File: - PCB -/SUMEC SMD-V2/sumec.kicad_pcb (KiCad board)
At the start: 2 copper layers, 48 parts, among them J1 Conn_01x04_Pin, J2 Conn_01x01_Pin, J3 Conn_01x03_Pin, J6 Conn_01x06_Pin, J7 Conn_01x06_Pin, J8 TSOP382xx, J9 Conn_01x06_Pin, SW1 SW_Push, SW2 SW_Push, SW3 SW_Push, SW4 SW_DPDT_x2, U1 TB6612FNG, U3 USBLC6-2SC6, U7 LM1084IS-5.0/NOPB, U8 LM1084IS-3.3/NOPB

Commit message: sumec SMD V2 schematic update
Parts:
- removed D2: 1N5819, Diode_SMD:D_1206_3216Metric
- removed J1: Conn_01x04_Pin, Connector_PinHeader_2.54mm:PinHeader_1x04_P2.54mm_Vertical
- removed J6, J7, J9: Conn_01x06_Pin, Connector_JST:JST_SH_BM06B-SRSS-TB_1x06-1MP_P1.00mm_Vertical
- removed J8: TSOP382xx, Connector_PinSocket_2.54mm:PinSocket_1x03_P2.54mm_Vertical
- removed JP1: SolderJumper_3_Open, Jumper:SolderJumper-3_P2.0mm_Open_TrianglePad1.0x1.5mm
- removed R10, R11, R12, R13, R4, R8, R9: 0R, Resistor_SMD:R_1206_3216Metric
- removed R14, R16, R18: 100, Resistor_SMD:R_1206_3216Metric
- removed R15, R17, R19: 10k, Resistor_SMD:R_1206_3216Metric
- removed R3: 220, Resistor_SMD:R_1206_3216Metric_Pad1.30x1.75mm_HandSolder
- removed R5, R6: 15R, Resistor_SMD:R_1206_3216Metric
- removed R7: 10k.mcu, Resistor_SMD:R_1206_3216Metric
- added C10: 10uF.stabl, Capacitor_SMD:CP_Elec_4x5.8, F.Cu at (127.2, 26.8)
- added C11: 10uF.stabl, Capacitor_SMD:CP_Elec_4x5.8, F.Cu at (127.2, 32.6)
- added C12: 10uF.stabl, Capacitor_SMD:CP_Elec_4x5.8, F.Cu at (127.2, 38.5)
- added C13: 10uF.stabl, Capacitor_SMD:CP_Elec_4x5.8, F.Cu at (127.2, 44.4)
- added IC1: XT30U-F, sumec-smdV2_library:XT30U-M_1x02_P5.0mm_Vertical, F.Cu at (127.0, 50.9)
- added J10: Conn_01x03_Pin, Connector_PinHeader_2.54mm:PinHeader_1x03_P2.54mm_Vertical, F.Cu at (126.2, 72.8)
- added J11: Conn_01x03_Pin, Connector_PinHeader_2.54mm:PinHeader_1x03_P2.54mm_Vertical, F.Cu at (130.8, 72.8)
- added J4: Conn_01x04_Pin, Connector_Molex:Molex_PicoBlade_53398-0471_1x04-1MP_P1.25mm_Vertical, F.Cu at (130.4, 66.4)
- added U4: MPU-9250, Sensor_Motion:InvenSense_QFN-24_3x3mm_P0.4mm, F.Cu at (135.8, 73.0)
- added U5: TSOP382xx, Connector_PinSocket_2.54mm:PinSocket_1x03_P2.54mm_Vertical, F.Cu at (139.2, 58.9)
- H1, H2, H3, H4: value MountingHole M3 -> MountingHole_Pad; footprint MountingHole:MountingHole_3.2mm_M3_ISO7380_Pad -> MountingHole:MountingHole_3.2mm_M3_Pad
- J3: value Conn_01x03_Pin -> Conn_01x04_Pin; footprint Connector_PinSocket_2.54mm:PinSocket_1x03_P2.54mm_Vertical -> Connector_Molex:Molex_PicoBlade_53398-0471_1x04-1MP_P1.25mm_Vertical
- moved SW4 92.3 mm to (100.2, 26.2)
- moved SW1 78.5 mm to (100.8, 35.8)
- moved J2 75.5 mm to (99.7, 39.8)
- moved H1 72.2 mm to (93.8, 27.9)
- moved H2 71.9 mm to (93.8, 35.8)
- moved H3 71.6 mm to (93.8, 43.8)
- moved U7 71.3 mm to (116.4, 30.1)
- moved U8 71.3 mm to (116.4, 42.4)
- moved H4 71.3 mm to (93.8, 51.7)
- moved J3 51.2 mm to (130.4, 59.5)
- moved U3 35.6 mm to (114.8, 77.5)
- moved SW2 35.6 mm to (114.2, 68.8)
- moved SW3 35.6 mm to (114.2, 73.1)
- moved U1 31.8 mm to (116.6, 61.5)
- moved D1 28.7 mm to (114.3, 81.4)
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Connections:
- H1 pad 1: (no net) -> GND
- H2 pad 1: (no net) -> GND
- H3 pad 1: (no net) -> GND
- H4 pad 1: (no net) -> GND
- J3 pad 2: GND -> +3V3
- J3 pad 3: +3V3 -> GND

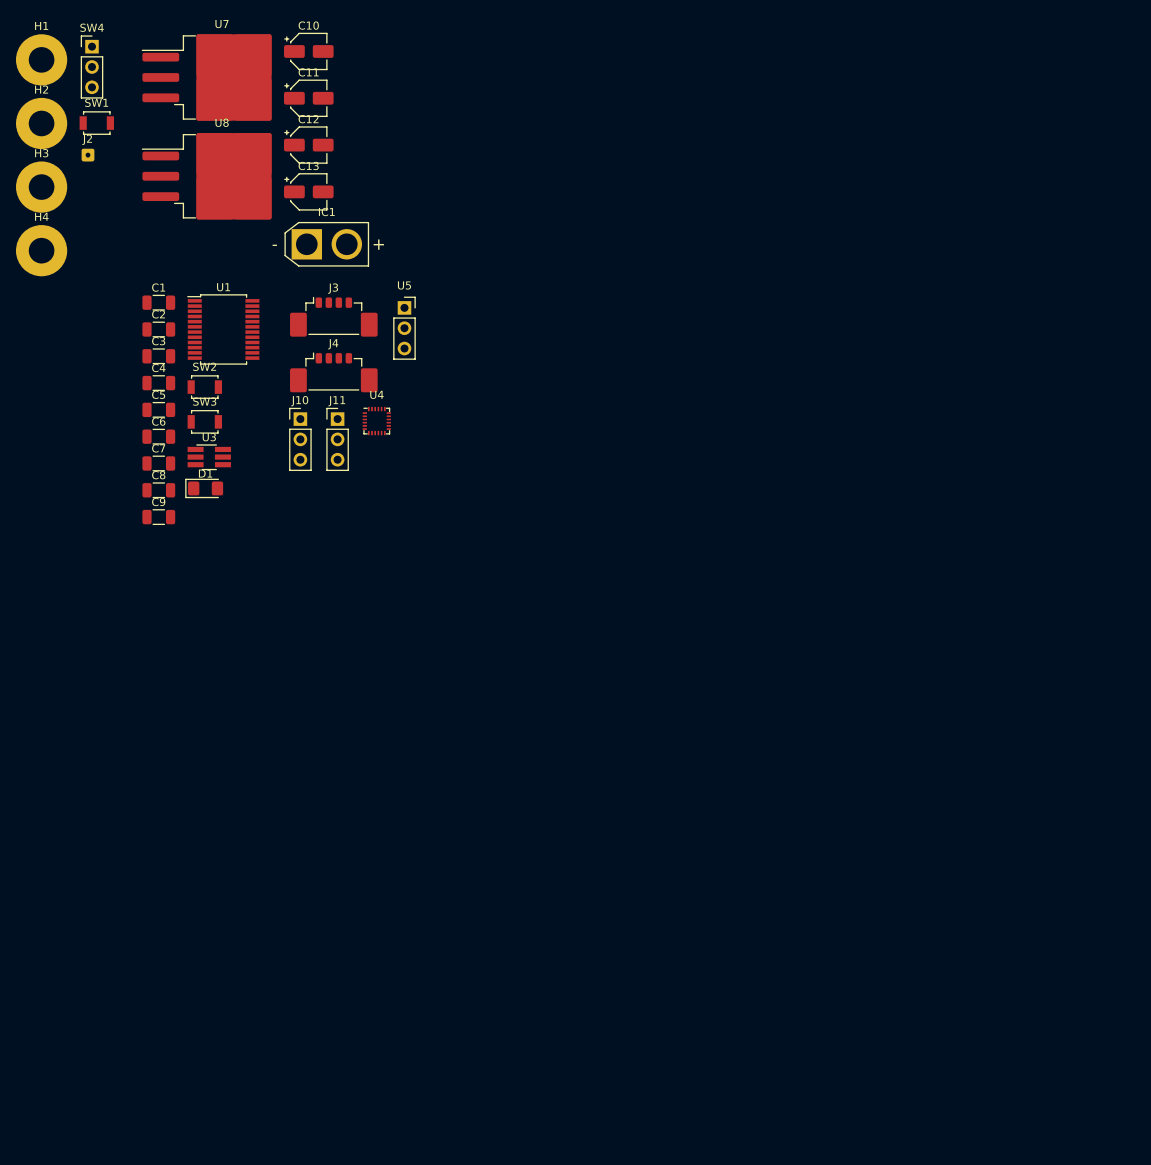
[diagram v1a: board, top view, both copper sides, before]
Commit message: SMDV2 - footprints
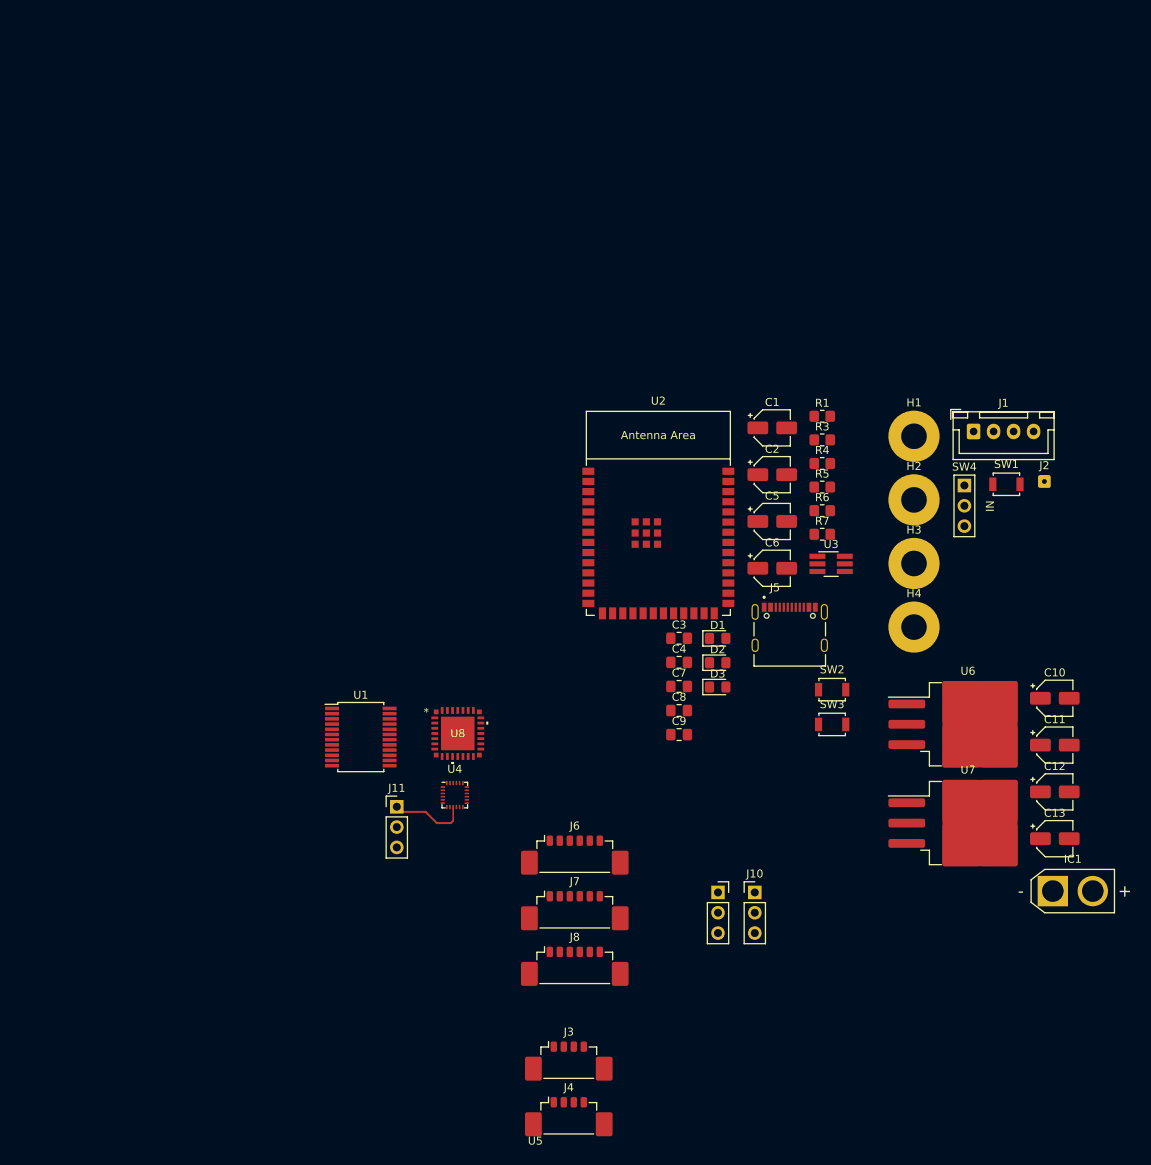
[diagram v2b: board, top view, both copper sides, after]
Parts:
- added D2: LED, LED_SMD:LED_0805_2012Metric_Pad1.15x1.40mm_HandSolder, F.Cu at (178.4, 103.2)
- added D3: D_Schottky, Diode_SMD:D_0805_2012Metric_Pad1.15x1.40mm_HandSolder, F.Cu at (178.4, 106.2)
- added J1: Conn_01x04_Pin, Connector_JST:JST_XH_B4B-XH-A_1x04_P2.50mm_Vertical, F.Cu at (210.3, 74.3)
- added J5: TYPE-C-31-M-12, sumec-smdV2_library:USB_Type_C, F.Cu at (187.4, 101.0)
- added J6: Conn_01x06_Pin, Connector_Molex:Molex_PicoBlade_53398-0671_1x06-1MP_P1.25mm_Vertical, F.Cu at (160.5, 126.7)
- added J7: Conn_01x06_Pin, Connector_Molex:Molex_PicoBlade_53398-0671_1x06-1MP_P1.25mm_Vertical, F.Cu at (160.5, 133.7)
- added J8: Conn_01x06_Pin, Connector_Molex:Molex_PicoBlade_53398-0671_1x06-1MP_P1.25mm_Vertical, F.Cu at (160.5, 140.6)
- added R1: 220, Resistor_SMD:R_0805_2012Metric_Pad1.20x1.40mm_HandSolder, F.Cu at (191.4, 72.4)
- added R3: 220, Resistor_SMD:R_0805_2012Metric_Pad1.20x1.40mm_HandSolder, F.Cu at (191.4, 75.3)
- added R4: 0R, Resistor_SMD:R_0805_2012Metric_Pad1.20x1.40mm_HandSolder, F.Cu at (191.4, 78.3)
- added R5: 15R, Resistor_SMD:R_0805_2012Metric_Pad1.20x1.40mm_HandSolder, F.Cu at (191.4, 81.2)
- added R6: 15R, Resistor_SMD:R_0805_2012Metric_Pad1.20x1.40mm_HandSolder, F.Cu at (191.4, 84.2)
- added R7: 10k.mcu, Resistor_SMD:R_0805_2012Metric_Pad1.20x1.40mm_HandSolder, F.Cu at (191.4, 87.2)
- added U2: ESP32-S3-WROOM-1, PCM_Espressif:ESP32-S3-WROOM-1, F.Cu at (170.9, 87.5)
- added U6: LM1084IS-5.0/NOPB, Package_TO_SOT_SMD:TO-263-3_TabPin4, F.Cu at (209.7, 110.9)
- C1, C2, C5, C6: footprint Capacitor_SMD:C_1206_3216Metric -> Capacitor_SMD:CP_Elec_4x5.8
- C3, C4, C7, C8, C9: footprint Capacitor_SMD:C_1206_3216Metric -> Capacitor_SMD:C_0805_2012Metric_Pad1.18x1.45mm_HandSolder
- D1: footprint LED_SMD:LED_1206_3216Metric_Pad1.42x1.75mm_HandSolder -> LED_SMD:LED_0805_2012Metric_Pad1.15x1.40mm_HandSolder
- SW4: footprint Connector_PinHeader_2.54mm:PinHeader_1x03_P2.54mm_Vertical -> sumec-smdV2_library:Custom_SPDT_Switch
- U7: value LM1084IS-5.0/NOPB -> LM1084IS-3.3/NOPB
- U8: value LM1084IS-3.3/NOPB -> TB9051FTG_EL; footprint Package_TO_SOT_SMD:TO-263-3_TabPin4 -> sumec-smdV2_library:P-QFN28-0606-0p65_TOS
- moved U7 131.8 mm to (209.7, 123.2)
- moved J2 126.3 mm to (219.2, 80.5)
- moved C10 123.4 mm to (220.5, 107.7)
- moved C11 123.4 mm to (220.5, 113.5)
- moved C12 123.4 mm to (220.5, 119.3)
- moved C13 123.4 mm to (220.5, 125.2)
- moved IC1 123.4 mm to (220.2, 131.8)
- moved SW1 122.3 mm to (214.4, 80.9)
- moved SW4 122.1 mm to (209.2, 81.0)
- moved H1 118.8 mm to (202.9, 74.9)
- moved H2 118.8 mm to (202.9, 82.8)
- moved H3 118.8 mm to (202.9, 90.8)
- moved H4 118.8 mm to (202.9, 98.8)
- moved J4 97.5 mm to (159.8, 159.4)
- moved J3 97.5 mm to (159.8, 152.4)
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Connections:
- D1 pad 2: LED -> TEST LED
- SW4 pad 1: VBATT -> +8V
- SW4 pad 2: +8V -> VBATT
- U4 pad 11: unconnected-(U4-FSYNC-Pad11) -> SHARP 2
- U4 pad 9: unconnected-(U4-AD0/MISO-Pad9) -> SHARP 2
- U7 pad 2: +5V -> +3V3
- U7 pad 3: +8V -> +5V
- U8 pad 1: GND -> unconnected-(U8-OCC-Pad1)
- U8 pad 2: +3V3 -> +5V
- U8 pad 3: +5V -> unconnected-(U8-ENB-Pad3)
- U8 pad 4: (no net) -> GND
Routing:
- net SHARP 2: track 0.00 -> 9.72 mm

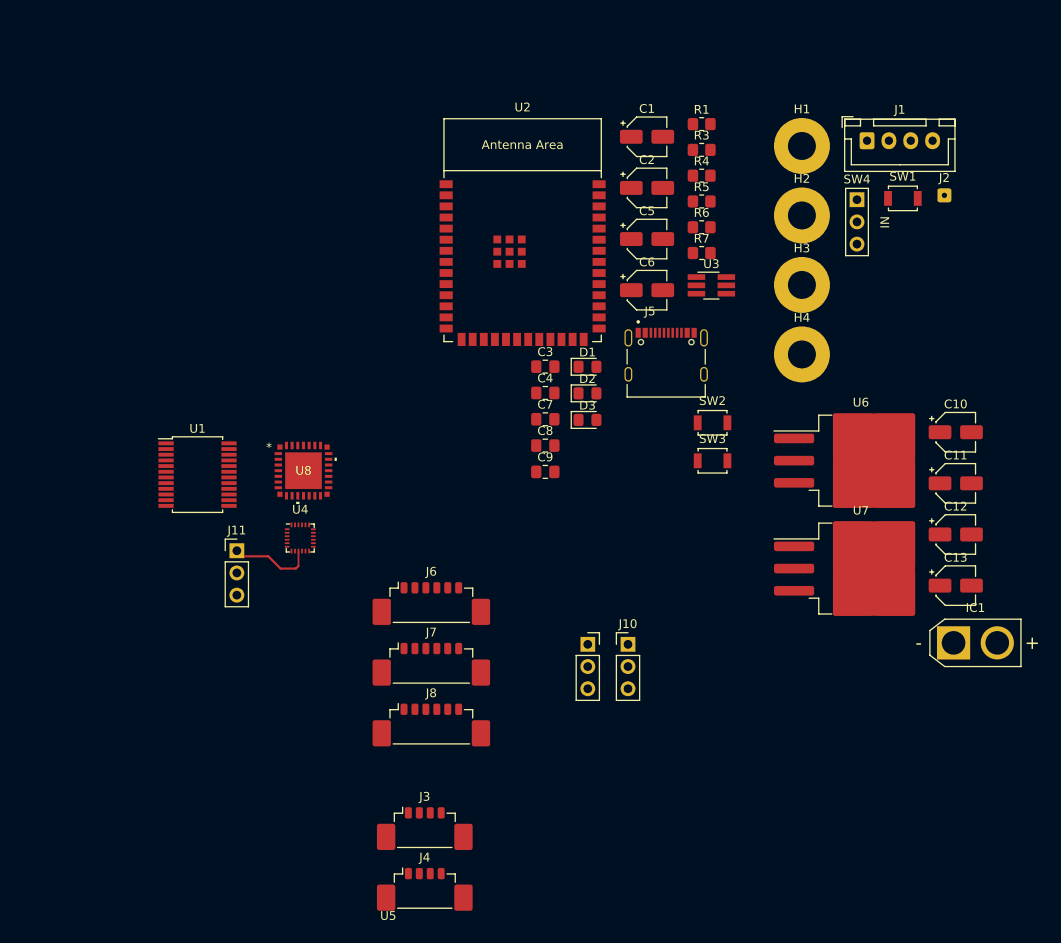
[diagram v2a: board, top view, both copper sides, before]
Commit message: Updates:
GyroScope project file, QRE1113 Board update and BOM, SMDv2 iBOM and schematic update.
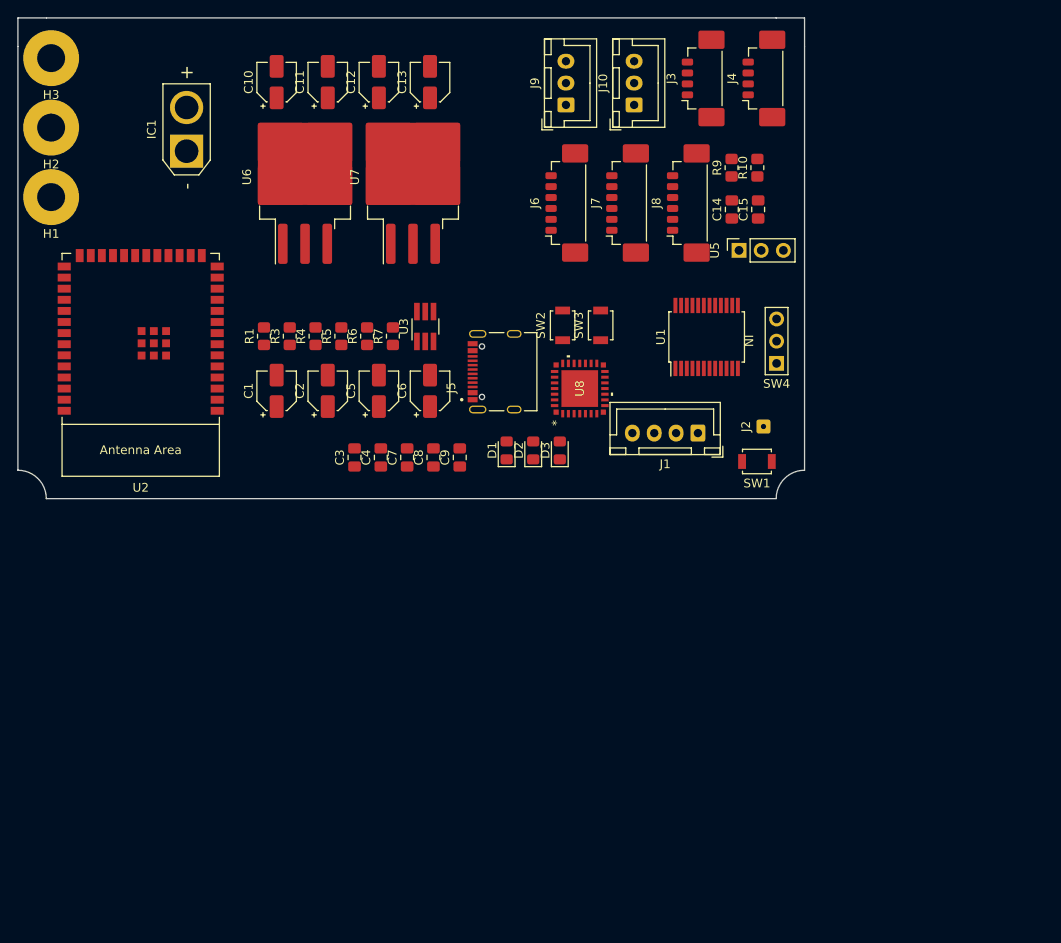
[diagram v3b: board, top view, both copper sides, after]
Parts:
- removed H4: MountingHole_Pad, MountingHole:MountingHole_3.2mm_M3_Pad
- removed J11: Conn_01x03_Pin, Connector_PinHeader_2.54mm:PinHeader_1x03_P2.54mm_Vertical
- removed U4: MPU-9250, Sensor_Motion:InvenSense_QFN-24_3x3mm_P0.4mm
- added C14: 10uF.shrp, Capacitor_SMD:C_0805_2012Metric_Pad1.18x1.45mm_HandSolder, F.Cu at (194.9, 82.2)
- added C15: 10uF.shrp, Capacitor_SMD:C_0805_2012Metric_Pad1.18x1.45mm_HandSolder, F.Cu at (197.9, 82.2)
- added J9: Conn_01x03_Pin, Connector_JST:JST_XH_B3B-XH-A_1x03_P2.50mm_Vertical, F.Cu at (175.9, 70.2)
- added R10: 100, Resistor_SMD:R_0805_2012Metric_Pad1.20x1.40mm_HandSolder, F.Cu at (197.8, 77.4)
- added R9: 10k, Resistor_SMD:R_0805_2012Metric_Pad1.20x1.40mm_HandSolder, F.Cu at (194.8, 77.4)
- J10: footprint Connector_PinHeader_2.54mm:PinHeader_1x03_P2.54mm_Vertical -> Connector_JST:JST_XH_B3B-XH-A_1x03_P2.50mm_Vertical
- moved IC1 104.2 mm to (132.5, 75.5), turned to 90 degrees
- moved J4 99.8 mm to (198.0, 67.2), turned to 90 degrees
- moved J3 90.8 mm to (191.1, 67.2), turned to 90 degrees
- moved H3 89.7 mm to (117.0, 64.8), turned to 180 degrees
- moved C10 87.4 mm to (142.8, 67.6), turned to 90 degrees
- moved H2 86.5 mm to (117.0, 72.8), turned to 180 degrees
- moved H1 86.1 mm to (117.0, 80.8), turned to 180 degrees
- moved C11 85.3 mm to (148.7, 67.6), turned to 90 degrees
- moved C12 83.9 mm to (154.5, 67.6), turned to 90 degrees
- moved C13 83.3 mm to (160.3, 67.6), turned to 90 degrees
- moved U6 71.4 mm to (146.1, 78.4), turned to 90 degrees
- moved U7 68.1 mm to (158.4, 78.4), turned to 90 degrees
- moved J8 65.8 mm to (189.3, 81.4), turned to 90 degrees
- moved J10 61.7 mm to (183.7, 70.2), turned to 90 degrees
- moved U1 60.3 mm to (192.0, 96.8), turned to 90 degrees
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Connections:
- net Net-(U8-OUT1-Pad13) renamed OUT1
- net Net-(U8-OUT2-Pad22) renamed OUT2
- J1 pad 3: MOTOR 2 - -> MOTOR 2 +
- J1 pad 4: MOTOR 2 + -> MOTOR 2 -
- J3 pad 1: QRE1113 A -> QRE1113 B
- J3 pad 4: QRE1113 B -> QRE1113 A
- J4 pad 2: +3V3 -> Net-(J4-Pin_2)
- U2 pad 32: unconnected-(U2-MTCK/GPIO39/CLK_OUT3/SUBSPICS1-Pad32) -> BUZZER
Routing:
- net SHARP 2: track 9.72 -> 0.00 mm
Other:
- board outline added: 90 x 55 mm

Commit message: SMDv2 Schematic update
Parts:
- removed U1: TB6612FNG, Package_SO:SSOP-24_5.3x8.2mm_P0.65mm
- removed U8: TB9051FTG_EL, sumec-smdV2_library:P-QFN28-0606-0p65_TOS
- added C16: 10uF.hb, Capacitor_SMD:CP_Elec_4x5.8, F.Cu at (245.0, 79.2)
- added C17: 100nF.hb, Capacitor_SMD:C_0805_2012Metric_Pad1.18x1.45mm_HandSolder, F.Cu at (239.4, 59.9)
- added C18: 22nF.hb, Capacitor_SMD:C_0805_2012Metric_Pad1.18x1.45mm_HandSolder, F.Cu at (239.4, 62.9)
- added C19: 220nF.hb, Capacitor_SMD:C_0805_2012Metric_Pad1.18x1.45mm_HandSolder, F.Cu at (239.4, 65.9)
- added IC2: DRV8874PWPR, sumec-smdV2_library:DRV8874, F.Cu at (236.6, 73.9)
- added IC3: DRV8874PWPR, sumec-smdV2_library:DRV8874, F.Cu at (236.6, 80.7)
- C1: value 10uF.hb -> 22nF.hb; footprint Capacitor_SMD:CP_Elec_4x5.8 -> Capacitor_SMD:C_0805_2012Metric_Pad1.18x1.45mm_HandSolder
- C2: value 1uF.hb -> 100nF.hb; footprint Capacitor_SMD:CP_Elec_4x5.8 -> Capacitor_SMD:C_0805_2012Metric_Pad1.18x1.45mm_HandSolder
- C5: value 10uF.hbc -> 10uF.hb
- C6: value 100nF.hbc -> 100nF.hb; footprint Capacitor_SMD:CP_Elec_4x5.8 -> Capacitor_SMD:C_0805_2012Metric_Pad1.18x1.45mm_HandSolder
- moved IC1 139.7 mm to (272.2, 79.4), turned to 0 degrees
- moved C10 130.2 mm to (272.4, 55.3), turned to 0 degrees
- moved C11 123.9 mm to (272.4, 61.1), turned to 0 degrees
- moved C12 117.9 mm to (272.4, 67.0), turned to 0 degrees
- moved U6 117.2 mm to (261.6, 58.5), turned to 0 degrees
- moved C13 112.2 mm to (272.4, 72.8), turned to 0 degrees
- moved R1 111.4 mm to (244.2, 53.9), turned to 0 degrees
- moved H3 109.5 mm to (215.4, 112.7), turned to 0 degrees
- moved R3 107.5 mm to (244.2, 56.8), turned to 0 degrees
- moved C1 104.1 mm to (234.6, 53.9), turned to 0 degrees
- moved R4 103.7 mm to (244.2, 59.8), turned to 0 degrees
- moved H2 103.5 mm to (215.4, 104.8), turned to 0 degrees
- moved U7 103.4 mm to (261.6, 70.9), turned to 0 degrees
- moved R5 99.9 mm to (244.2, 62.7), turned to 0 degrees
- moved H1 99.7 mm to (215.4, 96.8), turned to 0 degrees
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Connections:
- C1 pad 1: +3V3 -> Net-(IC3-CPL)
- C1 pad 2: GND -> Net-(IC3-CPH)
- C10 pad 1: +8V -> VM
- C2 pad 1: +3V3 -> VM
- C2 pad 2: GND -> Net-(IC3-VCP)
- C5 pad 1: +8V -> VM
- C6 pad 1: +8V -> GND
- C6 pad 2: GND -> VM
- J1 pad 1: MOTOR 1 + -> OUT 1A
- J1 pad 2: MOTOR 1 - -> OUT 1B
- J1 pad 3: MOTOR 2 + -> OUT 2A
- J1 pad 4: MOTOR 2 - -> OUT 2B
- SW4 pad 1: +8V -> VM
- U2 pad 17: AI2 -> unconnected-(U2-GPIO9/TOUCH9/ADC1_CH8/FSPIHD/SUBSPIHD-Pad17)
- U2 pad 18: AI1 -> unconnected-(U2-GPIO10/TOUCH10/ADC1_CH9/FSPICS0/FSPIIO4/SUBSPICS0-Pad18)
- U2 pad 19: PWMA -> IN1
- U2 pad 20: STBY -> PWM1
- U2 pad 21: BI1 -> IN2
- U2 pad 22: BI2 -> PWM2
- U2 pad 23: PWMB -> nSLEEP
- U2 pad 28: SHARP 2 -> unconnected-(U2-SPIIO6/GPIO35/FSPID/SUBSPID-Pad28)
- U2 pad 29: SHARP 1 -> unconnected-(U2-SPIIO7/GPIO36/FSPICLK/SUBSPICLK-Pad29)
- U2 pad 32: BUZZER -> SHARP 2
- U2 pad 33: X-SHUT1 -> SHARP 1
- U2 pad 34: X-SHUT2 -> unconnected-(U2-MTDI/GPIO41/CLK_OUT1-Pad34)
- U2 pad 35: X-SHUT3 -> unconnected-(U2-MTMS/GPIO42-Pad35)
- U2 pad 5: QRE1113 D -> QRE1113 B
- U2 pad 7: QRE1113 B -> unconnected-(U2-GPIO7/TOUCH7/ADC1_CH6-Pad7)
- U6 pad 3: +8V -> VM
